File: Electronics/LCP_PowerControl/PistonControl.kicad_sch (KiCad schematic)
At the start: 9 parts, among them U2 DRV8874

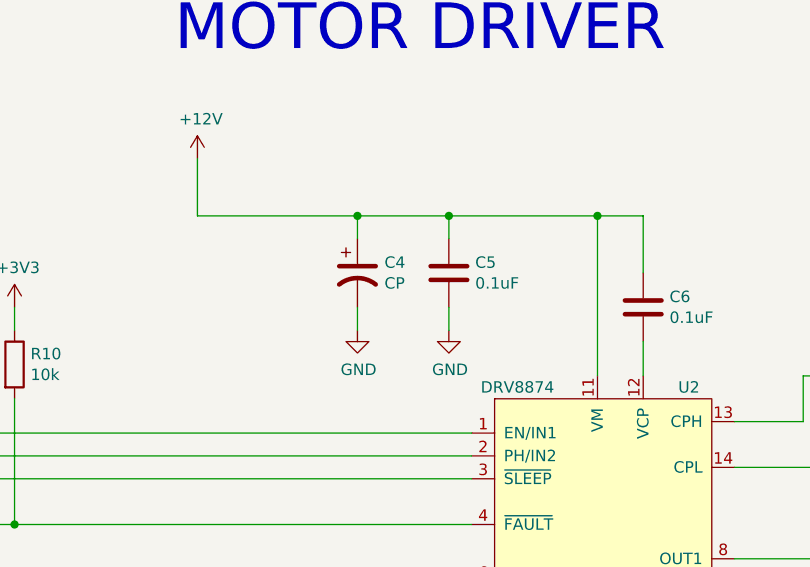
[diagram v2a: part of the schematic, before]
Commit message: vias around the inductor pad
per the LM61495 Datasheet
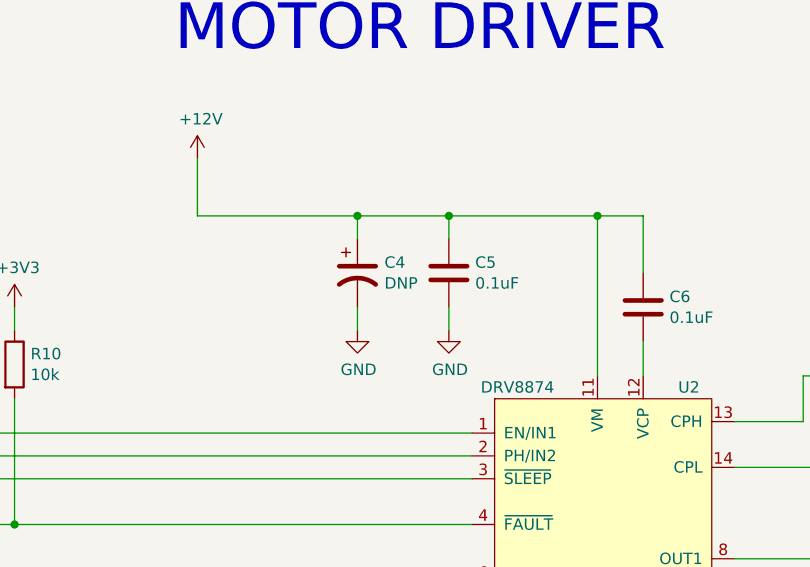
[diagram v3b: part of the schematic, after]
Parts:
- C4: value CP -> DNP
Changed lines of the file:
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@@
       (effects (font (size 1.27 1.27)) (justify left))
     )
-    (property "Value" "CP" (at 151.5872 64.643 0)
+    (property "Value" "DNP" (at 151.5872 64.643 0)
       (effects (font (size 1.27 1.27)) (justify left))
     )
